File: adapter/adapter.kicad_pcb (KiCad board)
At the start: 2 copper layers, 41.8 x 50.8 mm, 30 parts, among them J1 Serial, J2 Ribbon, J3 RGB, J4 Ribbon, J5 Battery charge, SW1 SW_SPST, SW3 SW_SPDT, U1 Dual MCU: RP2040 + nice!nano, U2 AP1603WG-7

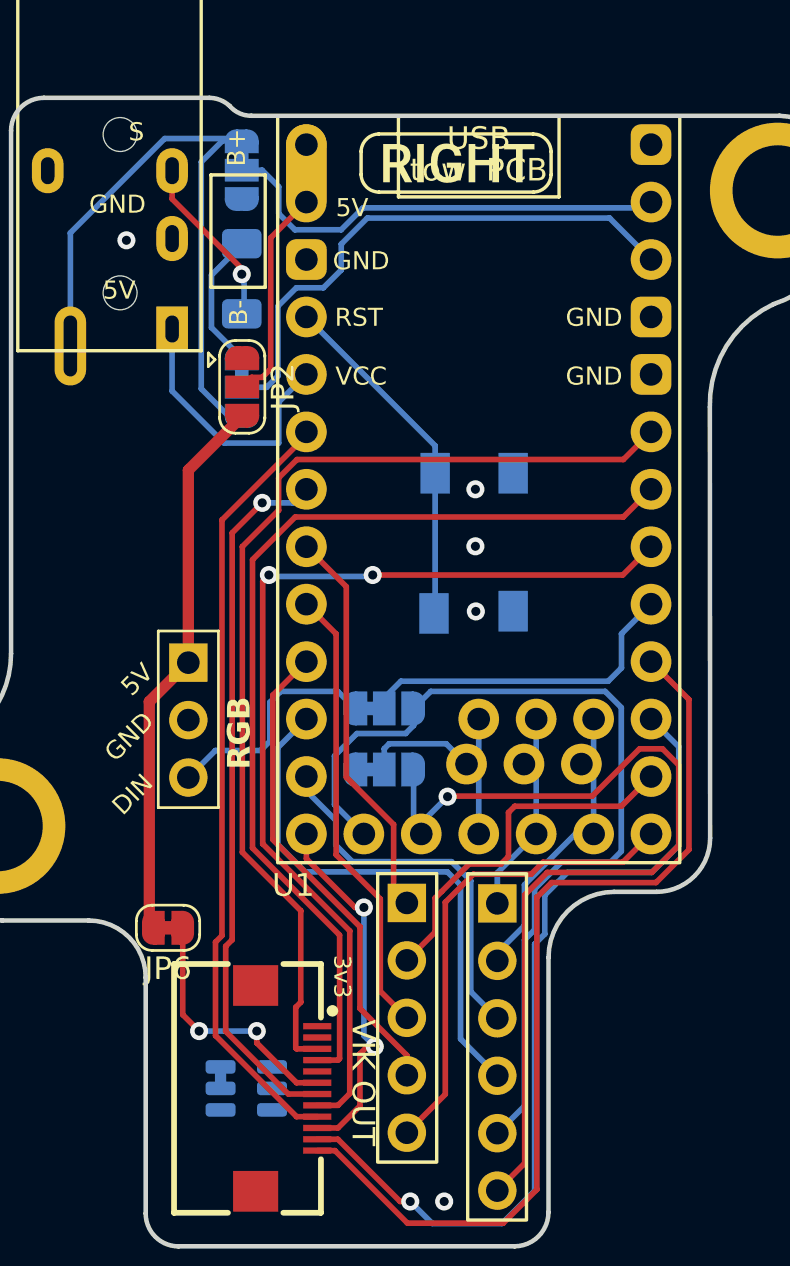
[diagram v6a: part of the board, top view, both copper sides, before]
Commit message: pcb: wire up 3v3 rgb and 5v
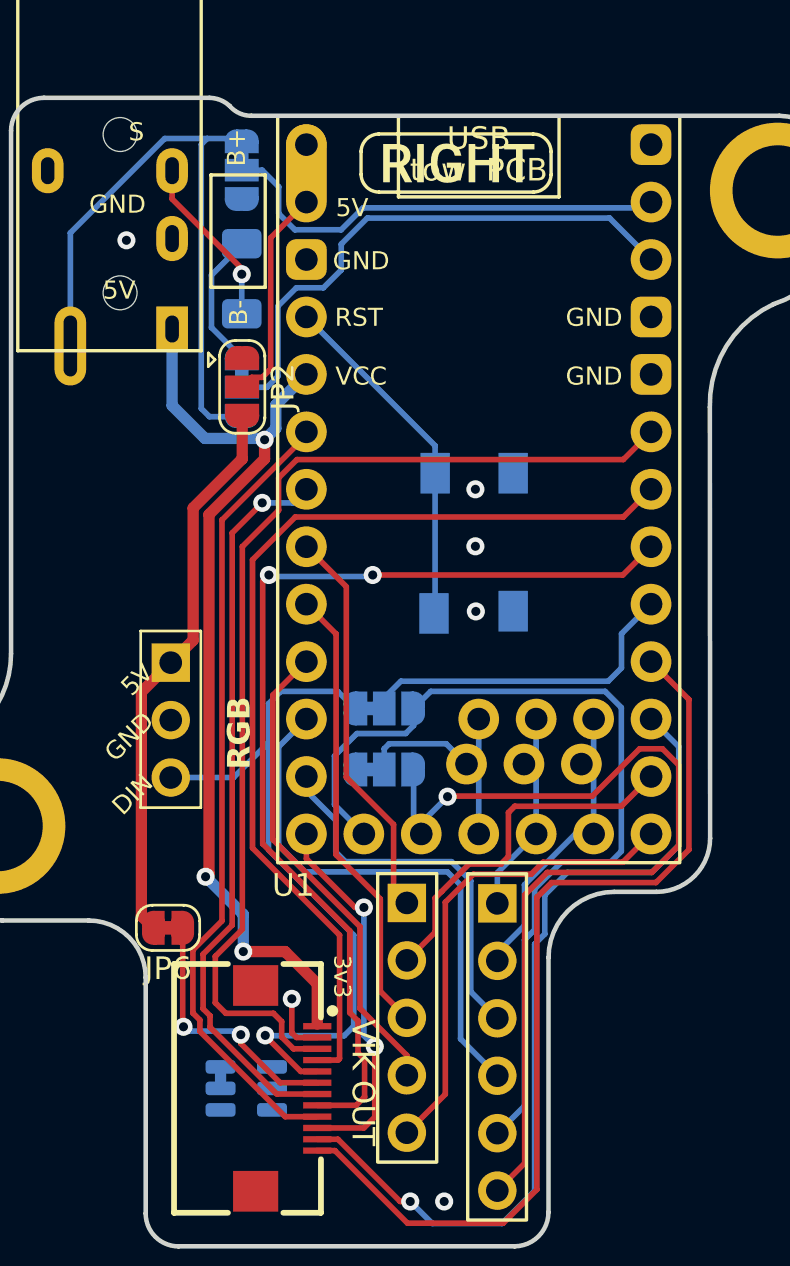
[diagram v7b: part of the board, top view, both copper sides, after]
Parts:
- moved J3 0.78 mm to (124.6, 92.2)
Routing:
- net +3V3: track 12.0 -> 41.8 mm, vias 0 -> 3
- net RGB_L: track 10.3 -> 31.6 mm, vias 0 -> 1
- net GND: track 1.15 -> 3.87 mm, vias 5 -> 6
- net SDA_L: track 45.3 -> 47.4 mm
- net GPIO_2_L: track 34.3 -> 35.5 mm
- net GPIO_1_L: track 31.4 -> 32.6 mm
- net MOSI_L: track 43.8 -> 44.8 mm
- net TX_L: track 29.1 -> 28.5 mm

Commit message: pcb: 3d models for headers
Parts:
- moved J5 15.9 mm to (121.5, 91.1), turned to -90 degrees
- moved SW3 15.0 mm to (119.4, 85.1), turned to -90 degrees
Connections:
- J5 pad 1: BAT_sw_l -> (no net)
- J5 pad 2: GND -> (no net)
- SW3 pad 1: unconnected-(SW3-A-Pad1) -> (no net)
- SW3 pad 2: B+_L -> (no net)
- SW3 pad 3: BAT_sw_l -> (no net)
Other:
- board text removed: "B+"
- board text removed: "B-"
